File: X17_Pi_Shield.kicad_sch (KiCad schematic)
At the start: 0 parts

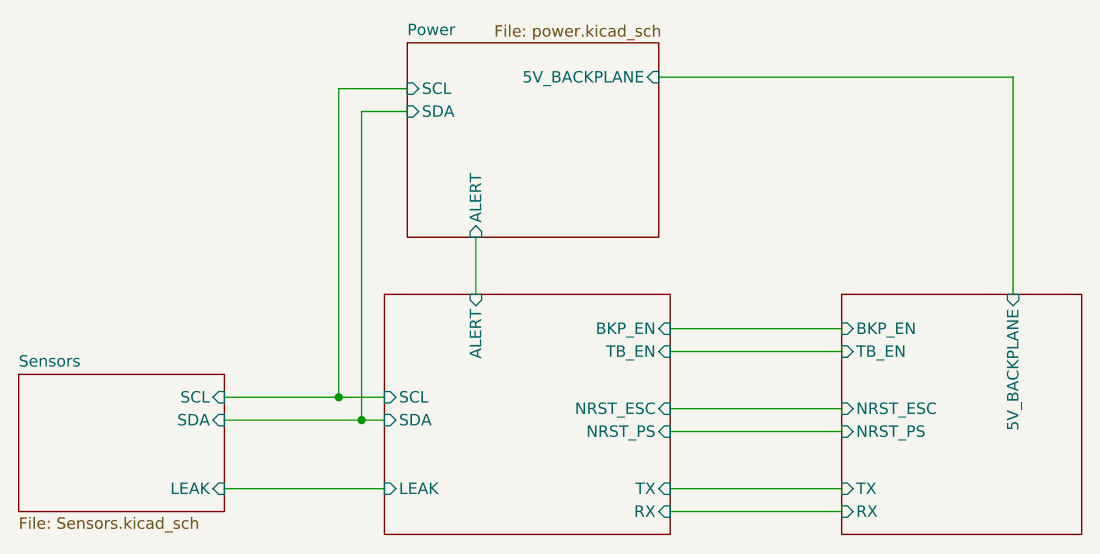
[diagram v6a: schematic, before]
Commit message: Updated Hiearchal Root Sheet
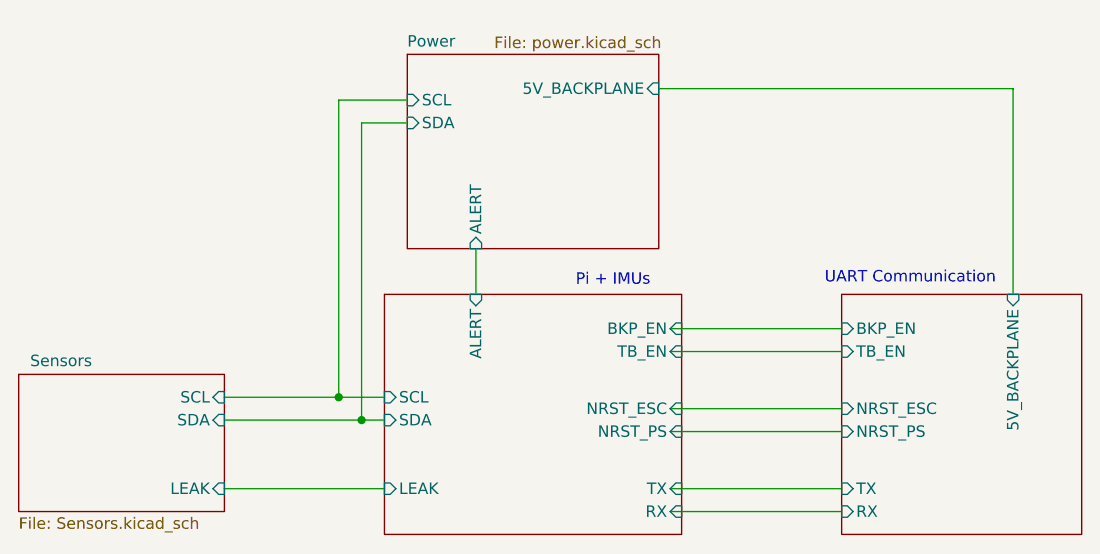
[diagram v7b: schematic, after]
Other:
- note added: "Pi + IMUs"
- note added: "UART Communication"
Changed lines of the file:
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@@
 	(wire
 		(pts
-			(xy 128.27 69.85) (xy 120.65 69.85)
-		)
-		(stroke
-			(width 0)
-			(type default)
-		)
-	)
-	(wire
-		(pts
-			(xy 195.58 68.58) (xy 195.58 92.71)
-		)
-		(stroke
-			(width 0)
-			(type default)
-		)
-	)
-	(wire
-		(pts
-			(xy 128.27 72.39) (xy 123.19 72.39)
+			(xy 128.27 71.12) (xy 120.65 71.12)
+		)
+		(stroke
+			(width 0)
+			(type default)
+		)
+	)
+	(wire
+		(pts
+			(xy 195.58 69.85) (xy 195.58 92.71)
+		)
+		(stroke
+			(width 0)
+			(type default)
+		)
+	)
+	(wire
+		(pts
+			(xy 128.27 73.66) (xy 123.19 73.66)
 		)
 		(stroke
@@
 	(wire
 		(pts
-			(xy 120.65 69.85) (xy 120.65 104.14)
+			(xy 120.65 71.12) (xy 120.65 104.14)
 		)
 		(stroke
@@
 	(wire
 		(pts
-			(xy 156.21 68.58) (xy 195.58 68.58)
+			(xy 156.21 69.85) (xy 195.58 69.85)
 		)
 		(stroke
@@
 	(wire
 		(pts
-			(xy 123.19 72.39) (xy 123.19 106.68)
+			(xy 123.19 73.66) (xy 123.19 106.68)
 		)
 		(stroke
@@
 	(wire
 		(pts
-			(xy 135.89 86.36) (xy 135.89 92.71)
+			(xy 135.89 87.63) (xy 135.89 92.71)
 		)
 		(stroke
@@
 			(width 0)
 			(type default)
+		)
+	)
+	(text "UART Communication"
+		(exclude_from_sim no)
+		(at 184.15 90.932 0)
+		(effects
+			(font
+				(size 1.27 1.27)
+			)
+		)
+	)
+	(text "Pi + IMUs"
+		(exclude_from_sim no)
+		(at 151.13 91.186 0)
+		(effects
+			(font
+				(size 1.27 1.27)
+			)
 		)
 	)
 	(sheet
 		(at 125.73 92.71)
-		(size 31.75 26.67)
+		(size 33.02 26.67)
 		(fields_autoplaced yes)
 		(stroke
@@
 		)
 		(pin "NRST_PS" input
-			(at 157.48 107.95 0)
+			(at 158.75 107.95 0)
 			(effects
 				(font
@@
 		)
 		(pin "NRST_ESC" input
-			(at 157.48 105.41 0)
+			(at 158.75 105.41 0)
 			(effects
 				(font
@@
 		)
 		(pin "TX" input
-			(at 157.48 114.3 0)
+			(at 158.75 114.3 0)
 			(effects
 				(font
@@
 		)
 		(pin "RX" input
-			(at 157.48 116.84 0)
+			(at 158.75 116.84 0)
 			(effects
 				(font
@@
 		)
 		(pin "TB_EN" input
-			(at 157.48 99.06 0)
+			(at 158.75 99.06 0)
 			(effects
 				(font
@@
 		)
 		(pin "BKP_EN" input
-			(at 157.48 96.52 0)
+			(at 158.75 96.52 0)
 			(effects
 				(font
@@
 		(at 85.09 101.6)
 		(size 22.86 15.24)
-		(fields_autoplaced yes)
 		(stroke
 			(width 0.1524)
@@
 		)
 		(property "Sheetname" "Sensors"
-			(at 85.09 100.8884 0)
+			(at 86.36 100.838 0)
 			(effects
 				(font
@@
 	)
 	(sheet
-		(at 128.27 64.77)
+		(at 128.27 66.04)
 		(size 27.94 21.59)
 		(stroke
@@
 		)
 		(property "Sheetname" "Power"
-			(at 128.27 64.0584 0)
+			(at 128.27 65.3284 0)
 			(effects
 				(font
@@
 		)
 		(property "Sheetfile" "power.kicad_sch"
-			(at 137.922 62.738 0)
+			(at 137.922 64.008 0)
 			(effects
 				(font
@@
 		)
 		(pin "5V_BACKPLANE" input
-			(at 156.21 68.58 0)
+			(at 156.21 69.85 0)
 			(effects
 				(font
@@
 		)
 		(pin "ALERT" input
-			(at 135.89 86.36 270)
+			(at 135.89 87.63 270)
 			(effects
 				(font
@@
 		)
 		(pin "SDA" input
-			(at 128.27 72.39 180)
+			(at 128.27 73.66 180)
 			(effects
 				(font
@@
 		)
 		(pin "SCL" input
-			(at 128.27 69.85 180)
-			(effects
-				(font
+			(at 128.27 71.12 180)
+			(effects
+				(font

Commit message: Pre-Toolbox Final
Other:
- sheet Pi + IMU ports: added RX_TB, TX_TB; removed none
- sheet UART ports: added RX_TB, TX_TB; removed none
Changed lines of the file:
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@@
+	(wire
+		(pts
+			(xy 158.75 105.41) (xy 176.53 105.41)
+		)
+		(stroke
+			(width 0)
+			(type default)
+		)
+	)
 	(wire
 		(pts
@@
 	(wire
 		(pts
+			(xy 158.75 99.06) (xy 176.53 99.06)
+		)
+		(stroke
+			(width 0)
+			(type default)
+		)
+	)
+	(wire
+		(pts
 			(xy 120.65 71.12) (xy 120.65 104.14)
 		)
@@
 	(wire
 		(pts
-			(xy 157.48 105.41) (xy 176.53 105.41)
-		)
-		(stroke
-			(width 0)
-			(type default)
-		)
-	)
-	(wire
-		(pts
 			(xy 156.21 69.85) (xy 195.58 69.85)
 		)
@@
 	(wire
 		(pts
-			(xy 157.48 96.52) (xy 176.53 96.52)
+			(xy 158.75 107.95) (xy 176.53 107.95)
+		)
+		(stroke
+			(width 0)
+			(type default)
+		)
+	)
+	(wire
+		(pts
+			(xy 158.75 123.19) (xy 176.53 123.19)
 		)
 		(stroke
@@
 	(wire
 		(pts
-			(xy 157.48 114.3) (xy 176.53 114.3)
-		)
-		(stroke
-			(width 0)
-			(type default)
-		)
-	)
-	(wire
-		(pts
-			(xy 157.48 107.95) (xy 176.53 107.95)
-		)
-		(stroke
-			(width 0)
-			(type default)
-		)
-	)
-	(wire
-		(pts
-			(xy 157.48 116.84) (xy 176.53 116.84)
+			(xy 158.75 120.65) (xy 176.53 120.65)
 		)
 		(stroke
@@
 	(wire
 		(pts
+			(xy 158.75 113.03) (xy 176.53 113.03)
+		)
+		(stroke
+			(width 0)
+			(type default)
+		)
+	)
+	(wire
+		(pts
 			(xy 107.95 106.68) (xy 123.19 106.68)
 		)
@@
 	(wire
 		(pts
-			(xy 157.48 99.06) (xy 176.53 99.06)
+			(xy 158.75 115.57) (xy 176.53 115.57)
+		)
+		(stroke
+			(width 0)
+			(type default)
+		)
+	)
+	(wire
+		(pts
+			(xy 158.75 96.52) (xy 176.53 96.52)
 		)
 		(stroke
@@
 	(sheet
 		(at 125.73 92.71)
-		(size 33.02 26.67)
+		(size 33.02 33.02)
 		(fields_autoplaced yes)
 		(stroke
@@
 		)
 		(property "Sheetfile" "pi_imu.kicad_sch"
-			(at 125.73 119.9646 0)
+			(at 125.73 126.3146 0)
 			(effects
 				(font
@@
 			)
 		)
-		(pin "TX" input
-			(at 158.75 114.3 0)
-			(effects
-				(font
-					(size 1.27 1.27)
-				)
-				(justify right)
-			)
-		)
 		(pin "RX" input
-			(at 158.75 116.84 0)
+			(at 158.75 123.19 0)
 			(effects
 				(font
@@
 		(pin "BKP_EN" input
 			(at 158.75 96.52 0)
+			(effects
+				(font
+					(size 1.27 1.27)
+				)
+				(justify right)
+			)
+		)
+		(pin "TX_TB" input
+			(at 158.75 113.03 0)
+			(effects
+				(font
+					(size 1.27 1.27)
+				)
+				(justify right)
+			)
+		)
+		(pin "RX_TB" input
+			(at 158.75 115.57 0)
+			(effects
+				(font
+					(size 1.27 1.27)
+				)
+				(justify right)
+			)
+		)
+		(pin "TX" input
+			(at 158.75 120.65 0)
 			(effects
 				(font
@@
 	(sheet
 		(at 176.53 92.71)
-		(size 26.67 26.67)
+		(size 26.67 31.75)
 		(fields_autoplaced yes)
 		(stroke
@@
 		)
 		(property "Sheetfile" "UART.kicad_sch"
-			(at 176.53 119.9646 0)
+			(at 176.53 125.0446 0)
 			(effects
 				(font
@@
 		)
 		(pin "RX" input
-			(at 176.53 116.84 180)
+			(at 176.53 123.19 180)
 			(effects
 				(font
@@
 		)
 		(pin "TX" input
-			(at 176.53 114.3 180)
+			(at 176.53 120.65 180)
 			(effects
 				(font
@@
 			)
 		)
+		(pin "RX_TB" input
+			(at 176.53 115.57 180)
+			(effects
+				(font
+					(size 1.27 1.27)
+				)
+				(justify left)
+			)
+		)
+		(pin "TX_TB" input
+			(at 176.53 113.03 180)
+			(effects
+				(font
+					(size 1.27 1.27)
+				)
+				(justify left)
+			)
+		)
